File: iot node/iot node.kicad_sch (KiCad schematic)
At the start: 19 parts

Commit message: update tekst
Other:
- note added: "button"
- note added: "buzzer"
- note added: "header"
- note added: "test led"
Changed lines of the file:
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@@
     (stroke (width 0) (type default) (color 0 0 0 0))
+  )
+  (text "header\n" (at 191.77 69.85 0)
+    (effects (font (size 1.27 1.27)) (justify left bottom))
+  )
+  (text "test led" (at 35.56 143.51 0)
+    (effects (font (size 1.27 1.27)) (justify left bottom))
+  )
+  (text "buzzer" (at 238.76 135.89 0)
+    (effects (font (size 1.27 1.27)) (justify left bottom))
+  )
+  (text "button" (at 36.83 146.05 0)
+    (effects (font (size 1.27 1.27)) (justify left bottom))
   )
   (global_label "RX" (shape input) (at 48.26 53.34 180) (fields_autoplaced)

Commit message: versie voor 2de sessie
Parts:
- added BZ1: Buzzer, symbol Device:Buzzer
- added C4, C5: 10u, symbol Device:C
- added C6: 0.1u, symbol Device:C
- added D2: LED, symbol Device:LED
- added J1: Conn_01x06_Female, symbol Connector:Conn_01x06_Female
- added J?: Conn_01x04_Female, symbol Connector:Conn_01x04_Female
- added R4, R5, R6: R, symbol Device:R
- added R9: 10k, symbol Device:R
- added SW5: SW_Push, symbol Switch:SW_Push
- added TP? (x15): TestPoint, symbol Connector:TestPoint
- added U3: NCP1117-3.3_SOT223, Package_TO_SOT_SMD:SOT-223-3_TabPin2, symbol Regulator_Linear:NCP1117-3.3_SOT223
- U1: renamed from U?; footprint MODULE_ESP32-WROOM-32E_(16MB) -> ESP32-WROOM-32E__16MB:MODULE_ESP32-WROOM-32E_(16MB)
- U5: renamed from U?; footprint PSON80P300X300X100-8N -> BME680:PSON80P300X300X100-8N
- gave numbers to parts that had none: 17
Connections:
- net 3.3: now also C5.2, J1.1 (Pin_1), J1.6 (Pin_6), J?.4 (Pin_4), TP?.1, TP?.1, TP?.1, U3.2 (VO)
- net GND: now also BZ1.2 (+), C4.1, C5.1, C6.1, J1.2 (Pin_2), J1.5 (Pin_5), J?.1 (Pin_1), R5.2, R6.2, R9.2, SW5.2, TP?.1, TP?.1, U3.1 (GND)
- net INT PIR: now also U2.4 (GPIO5/ADC2_CH0), R9.1, TP?.1
- net RX: now also J?.3 (Pin_3)
- net SCL: now also U2.17 (GPIO1/ADC1_CH1/XTAL_32K_N), J1.4 (Pin_4), TP?.1
- net SDA: now also U2.18 (GPIO0/ADC1_CH0/XTAL_32K_P), J1.3 (Pin_3), TP?.1
- net TX: now also J?.2 (Pin_2)
- net at U2.10 (GPIO10): now also TP?.1
- net batterij level: now reaches U2.15 (GPIO3/ADC1_CH3)
- net batterij level: now also R4.2, R5.1
- net buzzer+: now reaches U2.3 (GPIO4/ADC1_CH4)
- net buzzer+: now also BZ1.1 (-), TP?.1
- net test led: now reaches U2.5 (GPIO6)
- net test led: now also D2.2 (A), TP?.1
- net test button: now reaches U2.6 (GPIO7)
- net test button: now also C6.2, SW5.1, TP?.1
- net at U2.7 (GPIO8): now also TP?.1
- new net: D2.1 (K), R6.1
- new net + suply : C4.2, R4.1, U3.3 (VI)
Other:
- note removed: "buzzer"
- note removed: "header"

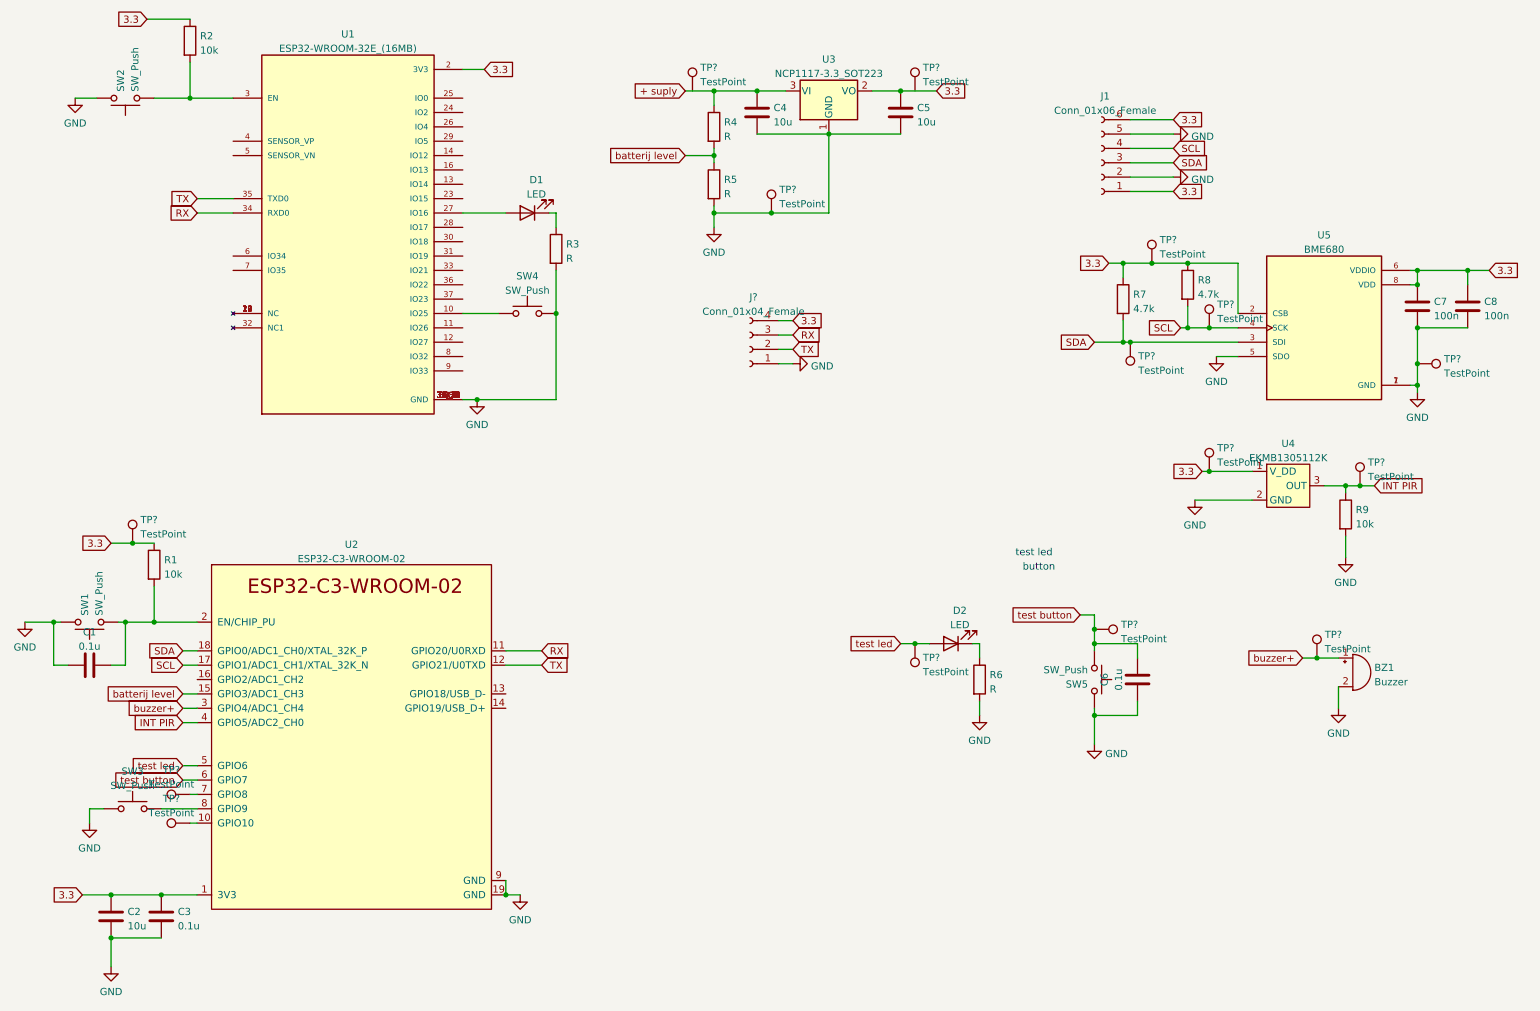
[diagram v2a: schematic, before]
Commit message: esp32 c3 bevesteging
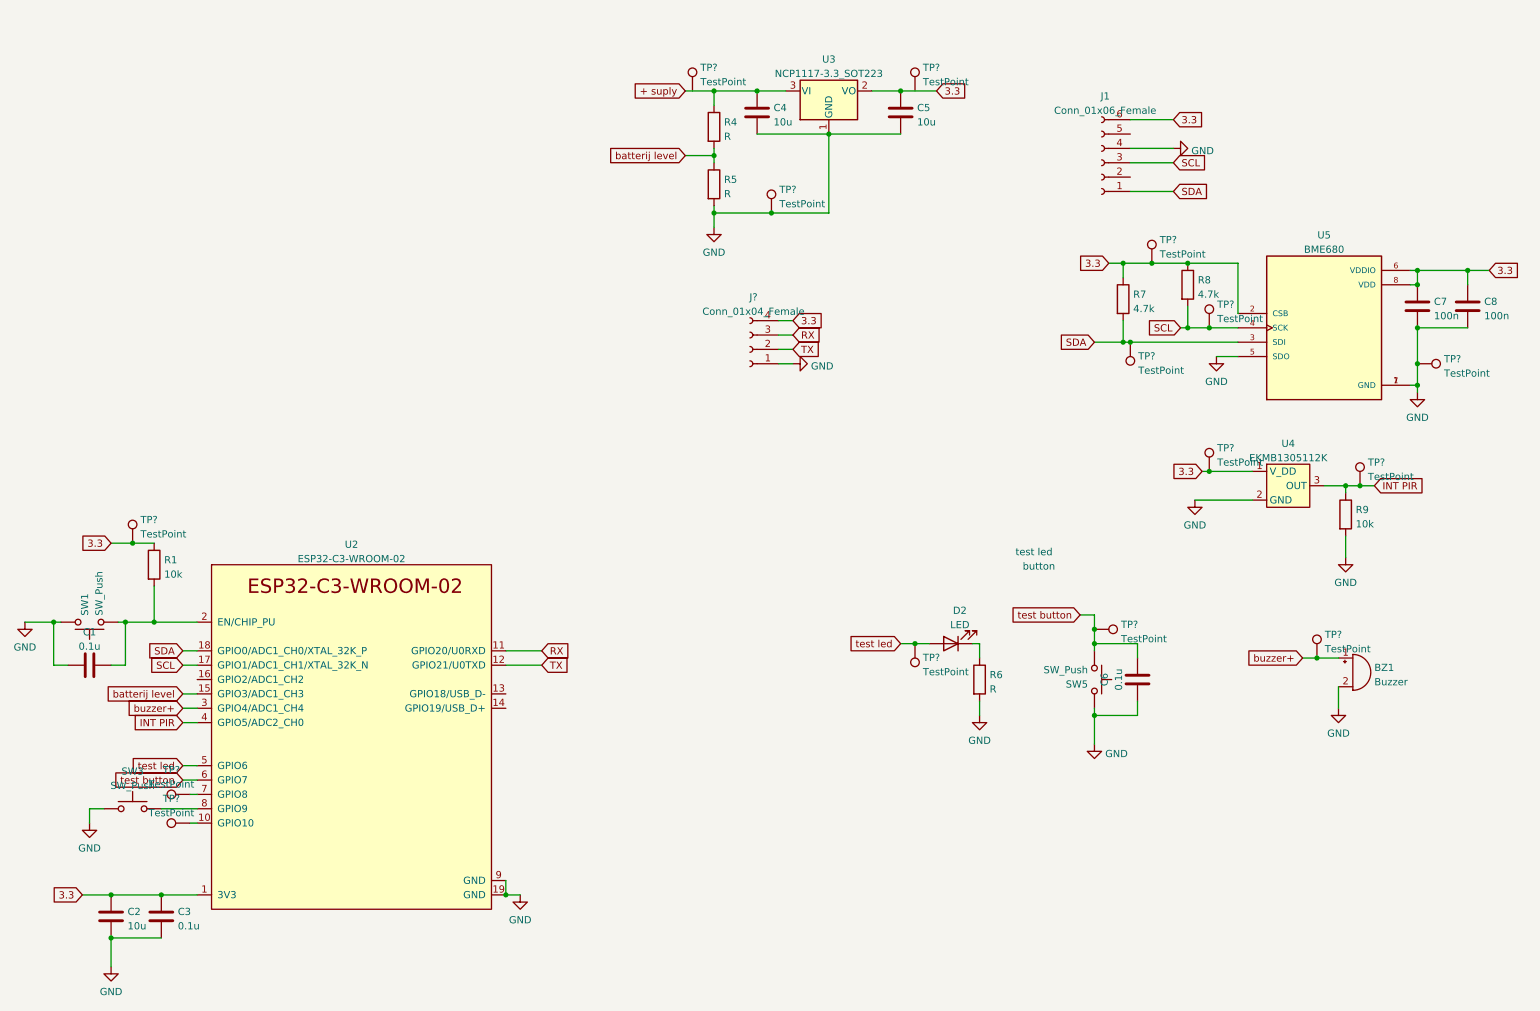
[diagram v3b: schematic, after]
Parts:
- removed D1: LED, symbol Device:LED
- removed R2: 10k, symbol Device:R
- removed R3: R, symbol Device:R
- removed SW2, SW4: SW_Push, symbol Switch:SW_Push
- removed U1: ESP32-WROOM-32E_(16MB), ESP32-WROOM-32E__16MB:MODULE_ESP32-WROOM-32E_(16MB), symbol ESP32-WROOM-32E__16MB_:ESP32-WROOM-32E_(16MB)
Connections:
- net 3.3: no longer J1.1 (Pin_1)
- net GND: now also J1.4 (Pin_4); no longer J1.2 (Pin_2), J1.5 (Pin_5)
- net SCL: now also J1.3 (Pin_3); no longer J1.4 (Pin_4)
- net SDA: now also J1.1 (Pin_1); no longer J1.3 (Pin_3)

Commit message: sessie 2
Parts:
- added R2: 4.7k, Resistor_SMD:R_0805_2012Metric_Pad1.20x1.40mm_HandSolder, symbol Device:R
- added X1: DG3XX-02-5.0, degson_DG306-5.0-02P, symbol degson:DG3XX-02-5.0
- BZ1: footprint (none) -> SamacSys_Parts:AX1203DLF
- C1, C2, C3, C4, C5, C6, C7, C8: footprint (none) -> Capacitor_SMD:C_0805_2012Metric_Pad1.18x1.45mm_HandSolder
- D1: renamed from D2; footprint (none) -> LED_SMD:LED_0805_2012Metric_Pad1.15x1.40mm_HandSolder
- J1: renamed from J?; footprint (none) -> Connector_PinSocket_2.54mm:PinSocket_1x04_P2.54mm_Vertical
- J2: renamed from J1; footprint (none) -> Connector_PinSocket_2.54mm:PinSocket_1x06_P2.54mm_Vertical
- R1: footprint (none) -> Resistor_SMD:R_0805_2012Metric_Pad1.20x1.40mm_HandSolder
- R3: renamed from R4; footprint (none) -> Resistor_SMD:R_0805_2012Metric_Pad1.20x1.40mm_HandSolder
- R4: renamed from R5; footprint (none) -> Resistor_SMD:R_0805_2012Metric_Pad1.20x1.40mm_HandSolder
- R5: renamed from R6; footprint (none) -> Resistor_SMD:R_0805_2012Metric_Pad1.20x1.40mm_HandSolder
- R6: renamed from R7; footprint (none) -> Resistor_SMD:R_0805_2012Metric_Pad1.20x1.40mm_HandSolder
- R7: renamed from R8; footprint (none) -> Resistor_SMD:R_0805_2012Metric_Pad1.20x1.40mm_HandSolder
- R8: renamed from R9; footprint (none) -> Resistor_SMD:R_0805_2012Metric_Pad1.20x1.40mm_HandSolder
- SW1: footprint (none) -> 434111043826:434111043826
- SW2: renamed from SW3; footprint (none) -> 434111043826:434111043826
- SW3: renamed from SW5; footprint (none) -> 434111043826:434111043826
- TP1, TP10, TP11, TP12, TP13, TP14, TP15, TP2, TP3, TP4, TP5, TP6, TP7, TP8, TP9: renamed from TP?; footprint (none) -> Connector_Pin:Pin_D1.0mm_L10.0mm
- U3: renamed from U4; footprint (none) -> Library:EKMB1305112K
- renumbered U2 to U1, U3 to U2, U5 to U4
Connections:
- net + suply : now also TP4.1, X1.1 (KL)
- net 3.3: now also TP6.1, R2.2
- net TX: now also R2.1
- net batterij level: now also X1.2 (KL)
- no-connect marks 0 -> 5

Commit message: versie 2 sessie2
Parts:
- U1: footprint Espressif:ESP32-C3-WROOM-02 -> esp:ESP32-C3-WROOM-02
- X1: footprint degson_DG306-5.0-02P -> degson:degson-DG306-5.0-02P
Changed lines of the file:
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@@
     (property "Reference" "U1" (id 0) (at 75.565 111.9972 0))
     (property "Value" "ESP32-C3-WROOM-02" (id 1) (at 75.565 114.5341 0))
-    (property "Footprint" "Espressif:ESP32-C3-WROOM-02" (id 2) (at 74.93 180.34 0)
+    (property "Footprint" "esp:ESP32-C3-WROOM-02" (id 2) (at 74.93 180.34 0)
       (effects (font (size 1.27 1.27)) hide)
     )
@@
       (effects (font (size 1.143 1.143)) (justify left bottom) hide)
     )
-    (property "Footprint" "degson_DG306-5.0-02P" (id 2) (at 139.7 46.482 0)
+    (property "Footprint" "degson:degson-DG306-5.0-02P" (id 2) (at 139.7 46.482 0)
       (effects (font (size 0.508 0.508)) hide)
     )
@@
       (effects (font (size 1.143 1.143)) (justify left bottom) hide)
     )
-    (property "Footprint" "degson_DG306-5.0-02P" (id 2) (at 140.97 35.052 0)
+    (property "Footprint" "degson:degson-DG306-5.0-02P" (id 2) (at 140.97 35.052 0)
       (effects (font (size 0.508 0.508)) hide)
     )
@@
     )
     (path "/05cdb9b6-c0dc-4fe6-92b4-e0c4062a70ca"
-      (reference "U1") (unit 1) (value "ESP32-C3-WROOM-02") (footprint "Espressif:ESP32-C3-WROOM-02")
+      (reference "U1") (unit 1) (value "ESP32-C3-WROOM-02") (footprint "esp:ESP32-C3-WROOM-02")
     )
     (path "/a3e9f845-898a-4c23-b17b-d34d86418e9b"
@@
     )
     (path "/fb5c3538-b4b0-4c6b-ba14-ef6c2ebf1f4d"
-      (reference "X1") (unit 1) (value "DG3XX-02-5.0") (footprint "degson_DG306-5.0-02P")
+      (reference "X1") (unit 1) (value "DG3XX-02-5.0") (footprint "degson:degson-DG306-5.0-02P")
     )
     (path "/92d34669-2c91-470a-98cf-019b45d8baf8"
-      (reference "X1") (unit 2) (value "DG3XX-02-5.0") (footprint "degson_DG306-5.0-02P")
-    )
-  )
+      (reference "X1") (unit 2) (value "DG3XX-02-5.0") (footprint "degson:degson-DG306-5.0-02P")
+    )
+  )

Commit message: Eerste PCB
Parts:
- TP1, TP10, TP11, TP12, TP13, TP14, TP15, TP2, TP3, TP4, TP5, TP6, TP7, TP8, TP9: footprint Connector_Pin:Pin_D1.0mm_L10.0mm -> Connector_Pin:Pin_D0.7mm_L6.5mm_W1.8mm_FlatFork
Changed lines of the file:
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@@
       (effects (font (size 1.27 1.27)) (justify right))
     )
-    (property "Footprint" "Connector_Pin:Pin_D1.0mm_L10.0mm" (id 2) (at 208.28 76.2 0)
+    (property "Footprint" "Connector_Pin:Pin_D0.7mm_L6.5mm_W1.8mm_FlatFork" (id 2) (at 208.28 76.2 0)
       (effects (font (size 1.27 1.27)) hide)
     )
@@
       (effects (font (size 1.27 1.27)) (justify left))
     )
-    (property "Footprint" "Connector_Pin:Pin_D1.0mm_L10.0mm" (id 2) (at 259.08 101.6 0)
+    (property "Footprint" "Connector_Pin:Pin_D0.7mm_L6.5mm_W1.8mm_FlatFork" (id 2) (at 259.08 101.6 0)
       (effects (font (size 1.27 1.27)) hide)
     )
@@
     (property "Reference" "TP2" (id 0) (at 43.688 151.8752 90))
     (property "Value" "TestPoint" (id 1) (at 43.688 154.4121 90))
-    (property "Footprint" "Connector_Pin:Pin_D1.0mm_L10.0mm" (id 2) (at 46.99 151.13 0)
+    (property "Footprint" "Connector_Pin:Pin_D0.7mm_L6.5mm_W1.8mm_FlatFork" (id 2) (at 46.99 151.13 0)
       (effects (font (size 1.27 1.27)) hide)
     )
@@
       (effects (font (size 1.27 1.27)) (justify left))
     )
-    (property "Footprint" "Connector_Pin:Pin_D1.0mm_L10.0mm" (id 2) (at 154.94 53.34 0)
+    (property "Footprint" "Connector_Pin:Pin_D0.7mm_L6.5mm_W1.8mm_FlatFork" (id 2) (at 154.94 53.34 0)
       (effects (font (size 1.27 1.27)) hide)
     )
@@
       (effects (font (size 1.27 1.27)) (justify left))
     )
-    (property "Footprint" "Connector_Pin:Pin_D1.0mm_L10.0mm" (id 2) (at 180.34 31.75 0)
+    (property "Footprint" "Connector_Pin:Pin_D0.7mm_L6.5mm_W1.8mm_FlatFork" (id 2) (at 180.34 31.75 0)
       (effects (font (size 1.27 1.27)) hide)
     )
@@
       (effects (font (size 1.27 1.27)) (justify left))
     )
-    (property "Footprint" "Connector_Pin:Pin_D1.0mm_L10.0mm" (id 2) (at 140.97 31.75 0)
+    (property "Footprint" "Connector_Pin:Pin_D0.7mm_L6.5mm_W1.8mm_FlatFork" (id 2) (at 140.97 31.75 0)
       (effects (font (size 1.27 1.27)) hide)
     )
@@
       (effects (font (size 1.27 1.27)) (justify left))
     )
-    (property "Footprint" "Connector_Pin:Pin_D1.0mm_L10.0mm" (id 2) (at 207.01 132.08 0)
+    (property "Footprint" "Connector_Pin:Pin_D0.7mm_L6.5mm_W1.8mm_FlatFork" (id 2) (at 207.01 132.08 0)
       (effects (font (size 1.27 1.27)) hide)
     )
@@
       (effects (font (size 1.27 1.27)) (justify left))
     )
-    (property "Footprint" "Connector_Pin:Pin_D1.0mm_L10.0mm" (id 2) (at 41.91 111.76 0)
+    (property "Footprint" "Connector_Pin:Pin_D0.7mm_L6.5mm_W1.8mm_FlatFork" (id 2) (at 41.91 111.76 0)
       (effects (font (size 1.27 1.27)) hide)
     )
@@
       (effects (font (size 1.27 1.27)) (justify left))
     )
-    (property "Footprint" "Connector_Pin:Pin_D1.0mm_L10.0mm" (id 2) (at 222.25 62.23 0)
+    (property "Footprint" "Connector_Pin:Pin_D0.7mm_L6.5mm_W1.8mm_FlatFork" (id 2) (at 222.25 62.23 0)
       (effects (font (size 1.27 1.27)) hide)
     )
@@
       (effects (font (size 1.27 1.27)) (justify left))
     )
-    (property "Footprint" "Connector_Pin:Pin_D1.0mm_L10.0mm" (id 2) (at 232.41 73.66 0)
+    (property "Footprint" "Connector_Pin:Pin_D0.7mm_L6.5mm_W1.8mm_FlatFork" (id 2) (at 232.41 73.66 0)
       (effects (font (size 1.27 1.27)) hide)
     )
@@
       (effects (font (size 1.27 1.27)) (justify left))
     )
-    (property "Footprint" "Connector_Pin:Pin_D1.0mm_L10.0mm" (id 2) (at 251.46 132.08 0)
+    (property "Footprint" "Connector_Pin:Pin_D0.7mm_L6.5mm_W1.8mm_FlatFork" (id 2) (at 251.46 132.08 0)
       (effects (font (size 1.27 1.27)) hide)
     )
@@
       (effects (font (size 1.27 1.27)) (justify right))
     )
-    (property "Footprint" "Connector_Pin:Pin_D1.0mm_L10.0mm" (id 2) (at 170.18 129.54 0)
+    (property "Footprint" "Connector_Pin:Pin_D0.7mm_L6.5mm_W1.8mm_FlatFork" (id 2) (at 170.18 129.54 0)
       (effects (font (size 1.27 1.27)) hide)
     )
@@
       (effects (font (size 1.27 1.27)) (justify left))
     )
-    (property "Footprint" "Connector_Pin:Pin_D1.0mm_L10.0mm" (id 2) (at 264.16 85.09 0)
+    (property "Footprint" "Connector_Pin:Pin_D0.7mm_L6.5mm_W1.8mm_FlatFork" (id 2) (at 264.16 85.09 0)
       (effects (font (size 1.27 1.27)) hide)
     )
@@
     (property "Reference" "TP3" (id 0) (at 43.688 156.9552 90))
     (property "Value" "TestPoint" (id 1) (at 43.688 159.4921 90))
-    (property "Footprint" "Connector_Pin:Pin_D1.0mm_L10.0mm" (id 2) (at 46.99 156.21 0)
+    (property "Footprint" "Connector_Pin:Pin_D0.7mm_L6.5mm_W1.8mm_FlatFork" (id 2) (at 46.99 156.21 0)
       (effects (font (size 1.27 1.27)) hide)
     )
@@
       (effects (font (size 1.27 1.27)) (justify left))
     )
-    (property "Footprint" "Connector_Pin:Pin_D1.0mm_L10.0mm" (id 2) (at 232.41 99.06 0)
+    (property "Footprint" "Connector_Pin:Pin_D0.7mm_L6.5mm_W1.8mm_FlatFork" (id 2) (at 232.41 99.06 0)
       (effects (font (size 1.27 1.27)) hide)
     )
@@
     )
     (path "/b39aa154-df2c-420f-b0d4-84dac7a147a3"
-      (reference "TP1") (unit 1) (value "TestPoint") (footprint "Connector_Pin:Pin_D1.0mm_L10.0mm")
+      (reference "TP1") (unit 1) (value "TestPoint") (footprint "Connector_Pin:Pin_D0.7mm_L6.5mm_W1.8mm_FlatFork")
     )
     (path "/3df36015-a94c-4021-9208-eb3e3e0ef9a5"
-      (reference "TP2") (unit 1) (value "TestPoint") (footprint "Connector_Pin:Pin_D1.0mm_L10.0mm")
+      (reference "TP2") (unit 1) (value "TestPoint") (footprint "Connector_Pin:Pin_D0.7mm_L6.5mm_W1.8mm_FlatFork")
     )
     (path "/ef38d6c8-2998-48f0-a5d2-9a8d56987346"
-      (reference "TP3") (unit 1) (value "TestPoint") (footprint "Connector_Pin:Pin_D1.0mm_L10.0mm")
+      (reference "TP3") (unit 1) (value "TestPoint") (footprint "Connector_Pin:Pin_D0.7mm_L6.5mm_W1.8mm_FlatFork")
     )
     (path "/8a495172-7daf-4d82-aaae-78e459663ba0"
-      (reference "TP4") (unit 1) (value "TestPoint") (footprint "Connector_Pin:Pin_D1.0mm_L10.0mm")
+      (reference "TP4") (unit 1) (value "TestPoint") (footprint "Connector_Pin:Pin_D0.7mm_L6.5mm_W1.8mm_FlatFork")
     )
     (path "/562f065a-f5b0-4ced-a4d5-2e1436e736e6"
-      (reference "TP5") (unit 1) (value "TestPoint") (footprint "Connector_Pin:Pin_D1.0mm_L10.0mm")
+      (reference "TP5") (unit 1) (value "TestPoint") (footprint "Connector_Pin:Pin_D0.7mm_L6.5mm_W1.8mm_FlatFork")
     )
     (path "/5f748c65-0a33-416f-bb78-9aef9b2dedb2"
-      (reference "TP6") (unit 1) (value "TestPoint") (footprint "Connector_Pin:Pin_D1.0mm_L10.0mm")
+      (reference "TP6") (unit 1) (value "TestPoint") (footprint "Connector_Pin:Pin_D0.7mm_L6.5mm_W1.8mm_FlatFork")
     )
     (path "/cf9eeffc-a0ca-4676-8e37-4b8f3921cd8b"
-      (reference "TP7") (unit 1) (value "TestPoint") (footprint "Connector_Pin:Pin_D1.0mm_L10.0mm")
+      (reference "TP7") (unit 1) (value "TestPoint") (footprint "Connector_Pin:Pin_D0.7mm_L6.5mm_W1.8mm_FlatFork")
     )
     (path "/8b94910a-d494-46d7-81ef-20b61a0fbc9d"
-      (reference "TP8") (unit 1) (value "TestPoint") (footprint "Connector_Pin:Pin_D1.0mm_L10.0mm")
+      (reference "TP8") (unit 1) (value "TestPoint") (footprint "Connector_Pin:Pin_D0.7mm_L6.5mm_W1.8mm_FlatFork")
     )
     (path "/3802c5fb-fbb8-4216-81b3-f399dfc252d1"
-      (reference "TP9") (unit 1) (value "TestPoint") (footprint "Connector_Pin:Pin_D1.0mm_L10.0mm")
+      (reference "TP9") (unit 1) (value "TestPoint") (footprint "Connector_Pin:Pin_D0.7mm_L6.5mm_W1.8mm_FlatFork")
     )
     (path "/b6999eb2-6e0f-47c7-a28a-0314cfadfaea"
-      (reference "TP10") (unit 1) (value "TestPoint") (footprint "Connector_Pin:Pin_D1.0mm_L10.0mm")
+      (reference "TP10") (unit 1) (value "TestPoint") (footprint "Connector_Pin:Pin_D0.7mm_L6.5mm_W1.8mm_FlatFork")
     )
     (path "/bebd45cd-fcfb-4345-99c7-93005e512918"
-      (reference "TP11") (unit 1) (value "TestPoint") (footprint "Connector_Pin:Pin_D1.0mm_L10.0mm")
+      (reference "TP11") (unit 1) (value "TestPoint") (footprint "Connector_Pin:Pin_D0.7mm_L6.5mm_W1.8mm_FlatFork")
     )
     (path "/f181baca-340c-4570-b197-b9647a3ba278"
-      (reference "TP12") (unit 1) (value "TestPoint") (footprint "Connector_Pin:Pin_D1.0mm_L10.0mm")
+      (reference "TP12") (unit 1) (value "TestPoint") (footprint "Connector_Pin:Pin_D0.7mm_L6.5mm_W1.8mm_FlatFork")
     )
     (path "/cab9d3f3-ba3f-4024-b3d6-87696cb91a7a"
-      (reference "TP13") (unit 1) (value "TestPoint") (footprint "Connector_Pin:Pin_D1.0mm_L10.0mm")
+      (reference "TP13") (unit 1) (value "TestPoint") (footprint "Connector_Pin:Pin_D0.7mm_L6.5mm_W1.8mm_FlatFork")
     )
     (path "/3a050439-7e3f-4a22-a5d5-2284b64c23f3"
-      (reference "TP14") (unit 1) (value "TestPoint") (footprint "Connector_Pin:Pin_D1.0mm_L10.0mm")
+      (reference "TP14") (unit 1) (value "TestPoint") (footprint "Connector_Pin:Pin_D0.7mm_L6.5mm_W1.8mm_FlatFork")
     )
     (path "/d5c27ca8-6666-42b1-a0ae-bd523da80071"
-      (reference "TP15") (unit 1) (value "TestPoint") (footprint "Connector_Pin:Pin_D1.0mm_L10.0mm")
+      (reference "TP15") (unit 1) (value "TestPoint") (footprint "Connector_Pin:Pin_D0.7mm_L6.5mm_W1.8mm_FlatFork")
     )
     (path "/05cdb9b6-c0dc-4fe6-92b4-e0c4062a70ca"
